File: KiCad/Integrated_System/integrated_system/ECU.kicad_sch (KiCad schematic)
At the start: 57 parts, among them J1 Jack-DC, J2 Fan 1, J3 Fan 2, J4 Fan 3, J6 Conn_02x04_Counter_Clockwise, Q1 BSS138, Q2 BSS138, Q3 BSS138, SW1 SW_SPDT, SW2 SW_SPDT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

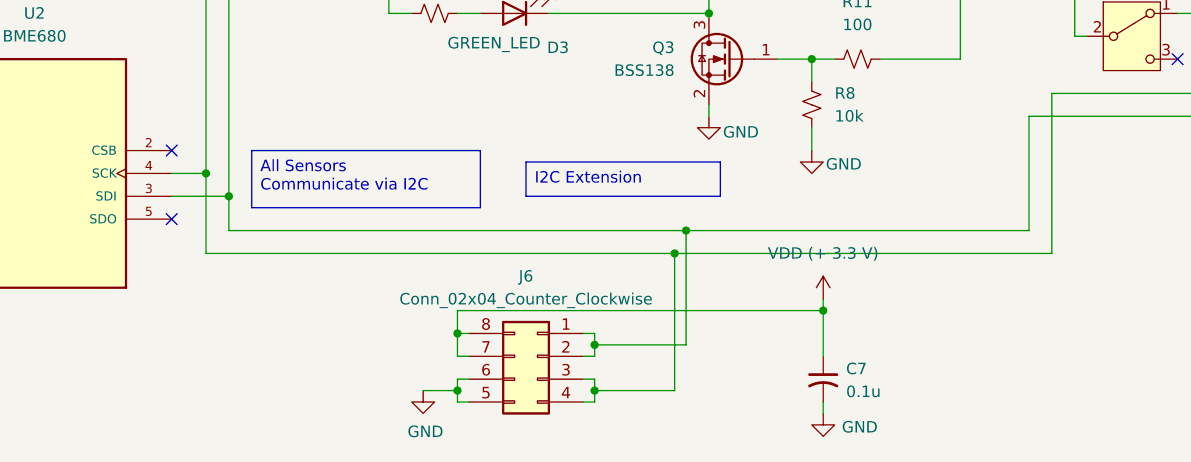
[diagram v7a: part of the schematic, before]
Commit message: added a ton of vias
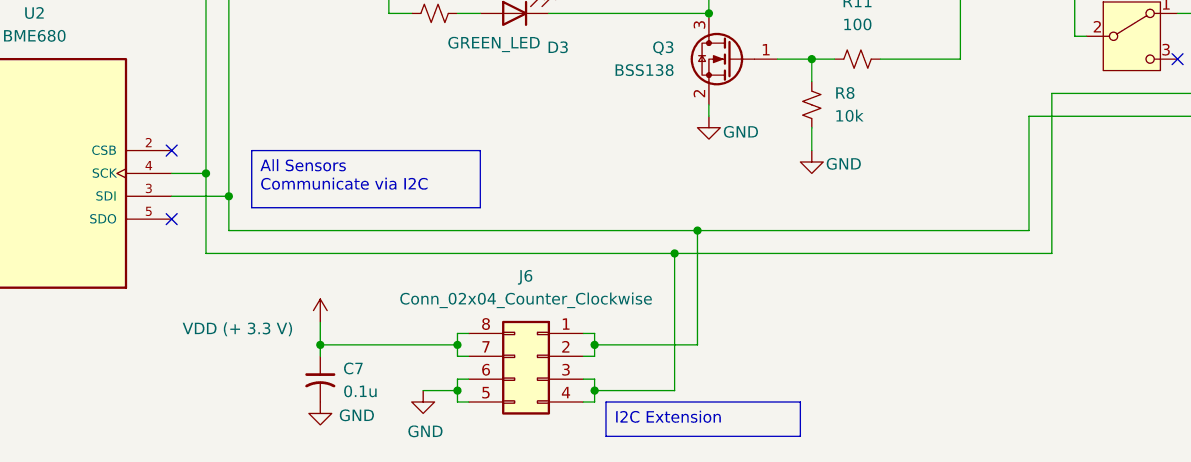
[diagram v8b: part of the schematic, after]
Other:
- moved on the sheet: C7
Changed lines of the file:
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@@
 	(text_box "I2C Extension"
 		(exclude_from_sim no)
-		(at 115.57 166.37 0)
+		(at 124.46 193.04 0)
 		(size 21.59 3.81)
 		(margins 0.9525 0.9525 0.9525 0.9525)
@@
 	)
 	(junction
-		(at 41.91 160.02)
+		(at 92.71 186.69)
 		(diameter 0)
 		(color 0 0 0 0)
 	)
 	(junction
-		(at 238.76 138.43)
+		(at 41.91 160.02)
 		(diameter 0)
 		(color 0 0 0 0)
 	)
 	(junction
-		(at 88.9 31.75)
+		(at 238.76 138.43)
 		(diameter 0)
 		(color 0 0 0 0)
 	)
 	(junction
-		(at 120.65 31.75)
+		(at 107.95 186.69)
 		(diameter 0)
 		(color 0 0 0 0)
 	)
 	(junction
-		(at 125.73 31.75)
+		(at 134.62 173.99)
 		(diameter 0)
 		(color 0 0 0 0)
 	)
 	(junction
-		(at 133.35 173.99)
+		(at 88.9 31.75)
 		(diameter 0)
 		(color 0 0 0 0)
 	)
 	(junction
-		(at 132.08 176.53)
+		(at 120.65 31.75)
 		(diameter 0)
 		(color 0 0 0 0)
 	)
 	(junction
-		(at 135.89 115.57)
+		(at 125.73 31.75)
 		(diameter 0)
 		(color 0 0 0 0)
 	)
 	(junction
-		(at 212.09 158.75)
+		(at 132.08 176.53)
 		(diameter 0)
 		(color 0 0 0 0)
 	)
 	(junction
-		(at 135.89 80.01)
+		(at 135.89 115.57)
 		(diameter 0)
 		(color 0 0 0 0)
 	)
 	(junction
-		(at 107.95 185.42)
+		(at 212.09 158.75)
 		(diameter 0)
 		(color 0 0 0 0)
 	)
 	(junction
-		(at 102.87 31.75)
+		(at 135.89 80.01)
 		(diameter 0)
 		(color 0 0 0 0)
 	)
 	(junction
-		(at 148.59 182.88)
+		(at 102.87 31.75)
 		(diameter 0)
 		(color 0 0 0 0)
@@
 	(wire
 		(pts
+			(xy 107.95 186.69) (xy 107.95 185.42)
+		)
+		(stroke
+			(width 0)
+			(type default)
+		)
+	)
+	(wire
+		(pts
 			(xy 50.8 34.29) (xy 50.8 26.67)
 		)
@@
 	(wire
 		(pts
+			(xy 92.71 184.15) (xy 92.71 186.69)
+		)
+		(stroke
+			(width 0)
+			(type default)
+		)
+	)
+	(wire
+		(pts
 			(xy 227.33 116.84) (xy 228.6 116.84)
 		)
@@
 	(wire
 		(pts
-			(xy 133.35 173.99) (xy 133.35 186.69)
+			(xy 134.62 173.99) (xy 134.62 186.69)
 		)
 		(stroke
@@
 	(wire
 		(pts
-			(xy 148.59 193.04) (xy 148.59 194.31)
-		)
-		(stroke
-			(width 0)
-			(type default)
-		)
-	)
-	(wire
-		(pts
 			(xy 107.95 190.5) (xy 107.95 191.77)
 		)
@@
 	(wire
 		(pts
-			(xy 107.95 182.88) (xy 107.95 185.42)
-		)
-		(stroke
-			(width 0)
-			(type default)
-		)
-	)
-	(wire
-		(pts
-			(xy 148.59 182.88) (xy 148.59 187.96)
-		)
-		(stroke
-			(width 0)
-			(type default)
-		)
-	)
-	(wire
-		(pts
 			(xy 173.99 119.38) (xy 173.99 123.19)
 		)
@@
 	(wire
 		(pts
-			(xy 107.95 187.96) (xy 107.95 185.42)
+			(xy 107.95 187.96) (xy 107.95 186.69)
 		)
 		(stroke
@@
 	(wire
 		(pts
+			(xy 92.71 186.69) (xy 107.95 186.69)
+		)
+		(stroke
+			(width 0)
+			(type default)
+		)
+	)
+	(wire
+		(pts
 			(xy 205.74 27.94) (xy 205.74 31.75)
 		)
@@
 	(wire
 		(pts
-			(xy 148.59 181.61) (xy 148.59 182.88)
-		)
-		(stroke
-			(width 0)
-			(type default)
-		)
-	)
-	(wire
-		(pts
 			(xy 107.95 149.86) (xy 110.49 149.86)
 		)
@@
 	(wire
 		(pts
-			(xy 123.19 186.69) (xy 133.35 186.69)
+			(xy 123.19 186.69) (xy 134.62 186.69)
 		)
 		(stroke
@@
 	(wire
 		(pts
-			(xy 133.35 173.99) (xy 171.45 173.99)
-		)
-		(stroke
-			(width 0)
-			(type default)
-		)
-	)
-	(wire
-		(pts
 			(xy 241.3 92.71) (xy 246.38 92.71)
 		)
@@
 	(wire
 		(pts
+			(xy 134.62 173.99) (xy 171.45 173.99)
+		)
+		(stroke
+			(width 0)
+			(type default)
+		)
+	)
+	(wire
+		(pts
 			(xy 135.89 137.16) (xy 135.89 138.43)
 		)
@@
 	(wire
 		(pts
-			(xy 107.95 182.88) (xy 148.59 182.88)
-		)
-		(stroke
-			(width 0)
-			(type default)
-		)
-	)
-	(wire
-		(pts
 			(xy 74.93 31.75) (xy 88.9 31.75)
 		)
@@
 	(wire
 		(pts
+			(xy 92.71 187.96) (xy 92.71 186.69)
+		)
+		(stroke
+			(width 0)
+			(type default)
+		)
+	)
+	(wire
+		(pts
 			(xy 129.54 74.93) (xy 135.89 74.93)
 		)
@@
 	(wire
 		(pts
-			(xy 82.55 173.99) (xy 133.35 173.99)
+			(xy 82.55 173.99) (xy 134.62 173.99)
 		)
 		(stroke
@@
 	(symbol
 		(lib_id "Device:C_Small_US")
-		(at 148.59 190.5 0)
+		(at 92.71 190.5 0)
 		(unit 1)
 		(exclude_from_sim no)
@@
 		(fields_autoplaced yes)
 		(property "Reference" "C7"
-			(at 151.13 189.3569 0)
+			(at 95.25 189.3569 0)
 			(effects
 				(font
@@
 		)
 		(property "Value" "0.1u"
-			(at 151.13 191.8969 0)
+			(at 95.25 191.8969 0)
 			(effects
 				(font
@@
 		)
 		(property "Footprint" "Capacitor_SMD:C_1206_3216Metric_Pad1.33x1.80mm_HandSolder"
-			(at 148.59 190.5 0)
+			(at 92.71 190.5 0)
 			(effects
 				(font
@@
 		)
 		(property "Datasheet" ""
-			(at 148.59 190.5 0)
+			(at 92.71 190.5 0)
 			(effects
 				(font
@@
 		)
 		(property "Description" "capacitor, small US symbol"
-			(at 148.59 190.5 0)
+			(at 92.71 190.5 0)
 			(effects
 				(font
@@
 	(symbol
 		(lib_id "power:+12V")
-		(at 148.59 181.61 0)
+		(at 92.71 184.15 0)
 		(unit 1)
 		(exclude_from_sim no)
@@
 		(on_board yes)
 		(dnp no)
-		(fields_autoplaced yes)
 		(property "Reference" "#PWR012"
-			(at 148.59 185.42 0)
+			(at 92.71 187.96 0)
 			(effects
 				(font
@@
 		)
 		(property "Value" "VDD (+ 3.3 V)"
-			(at 148.59 176.53 0)
+			(at 83.566 184.912 0)
 			(effects
 				(font
@@
 		)
 		(property "Footprint" ""
-			(at 148.59 181.61 0)
+			(at 92.71 184.15 0)
 			(effects
 				(font
@@
 		)
 		(property "Datasheet" ""
-			(at 148.59 181.61 0)
+			(at 92.71 184.15 0)
 			(effects
 				(font
@@
 		)
 		(property "Description" "Power symbol creates a global label with name \"+12V\""
-			(at 148.59 181.61 0)
+			(at 92.71 184.15 0)
 			(effects
 				(font
@@
 	(symbol
 		(lib_id "power:GND")
-		(at 148.59 194.31 0)
+		(at 92.71 193.04 0)
 		(unit 1)
 		(exclude_from_sim no)
@@
 		(dnp no)
 		(property "Reference" "#PWR014"
-			(at 148.59 200.66 0)
+			(at 92.71 199.39 0)
 			(effects
 				(font
@@
 		)
 		(property "Value" "GND"
-			(at 152.654 195.834 0)
+			(at 96.774 194.564 0)
 			(effects
 				(font
@@
 		)
 		(property "Footprint" ""
-			(at 148.59 194.31 0)
+			(at 92.71 193.04 0)
 			(effects
 				(font
@@
 		)
 		(property "Datasheet" ""
-			(at 148.59 194.31 0)
+			(at 92.71 193.04 0)
 			(effects
 				(font
@@
 		)
 		(property "Description" "Power symbol creates a global label with name \"GND\" , ground"
-			(at 148.59 194.31 0)
+			(at 92.71 193.04 0)
 			(effects
 				(font
